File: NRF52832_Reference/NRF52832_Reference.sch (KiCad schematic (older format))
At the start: 49 parts

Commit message: Added breakout pins for SWDIO and SWDCLK for test purposes.
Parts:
- added J?: Conn_01x02_Male, symbol Connector:Conn_01x02_Male
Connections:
- net Sheet5BF15571/SWDCLK renamed SWDCLK
- net SWDCLK: now also J?.2 (Pin_2)
- net Sheet5BF15571/SWDIO renamed SWDIO
- net SWDIO: now also J?.1 (Pin_1)
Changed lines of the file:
@@
 NoConn ~ 7875 3800
 Wire Wire Line
-	9625 4300 9625 3600
+	9625 4300 9625 3675
 Wire Wire Line
 	9325 4300 9175 4300
@@
 Connection ~ 9625 4300
 Wire Wire Line
-	9750 5100 9750 3500
+	9750 5100 9750 3775
 Wire Notes Line
 	475  2575 11225 2575
@@
 Text Notes 3900 650  0    50   ~ 0
 GPIO and Button/LEDs
+$Comp
+L Connector:Conn_01x02_Male J?
+U 1 1 5C377AB0
+P 10475 3775
+F 0 "J?" H 10447 3701 50  0000 R CNN
+F 1 "Conn_01x02_Male" H 10448 3746 50  0001 R CNN
+F 2 "" H 10475 3775 50  0001 C CNN
+F 3 "~" H 10475 3775 50  0001 C CNN
+	1    10475 3775
+	-1   0    0    1
+$EndComp
+Wire Wire Line
+	10275 3675 9625 3675
+Connection ~ 9625 3675
+Wire Wire Line
+	9625 3675 9625 3600
+Wire Wire Line
+	10275 3775 9750 3775
+Connection ~ 9750 3775
+Wire Wire Line
+	9750 3775 9750 3500
+Text Label 9850 3675 0    50   ~ 0
+SWDCLK
+Text Label 9850 3775 0    50   ~ 0
+SWDIO
 $EndSCHEMATC

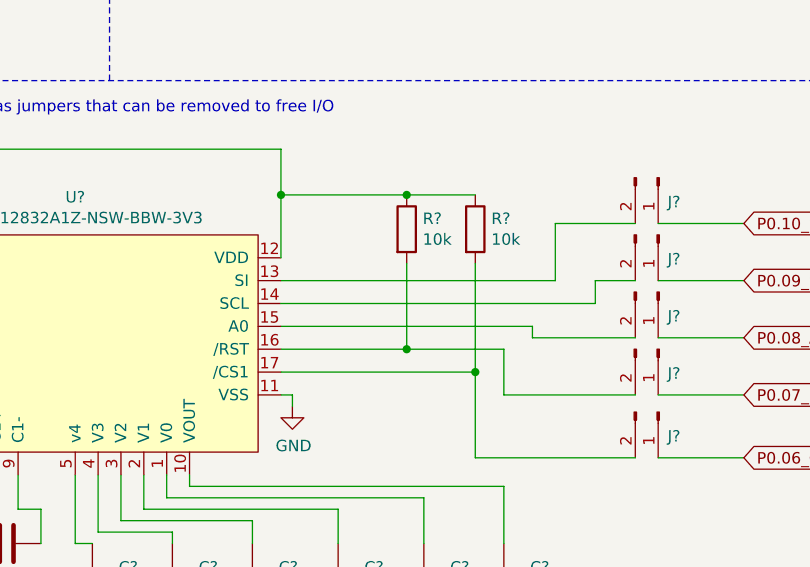
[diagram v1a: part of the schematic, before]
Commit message: Finished boost converter and regulators footprint assignments.
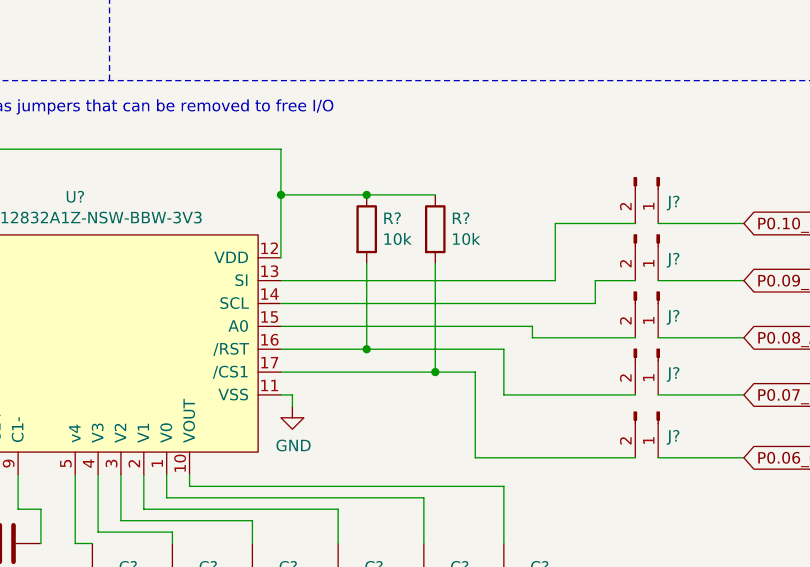
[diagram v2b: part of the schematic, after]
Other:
- moved on the sheet: R?
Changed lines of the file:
@@
 L Device:R R?
 U 1 1 5C0CAB0C
-P 4175 3225
-F 0 "R?" H 4245 3271 50  0000 L CNN
-F 1 "10k" H 4245 3180 50  0000 L CNN
-F 2 "" V 4105 3225 50  0001 C CNN
-F 3 "~" H 4175 3225 50  0001 C CNN
-	1    4175 3225
+P 4000 3225
+F 0 "R?" H 4070 3271 50  0000 L CNN
+F 1 "10k" H 4070 3180 50  0000 L CNN
+F 2 "" V 3930 3225 50  0001 C CNN
+F 3 "~" H 4000 3225 50  0001 C CNN
+	1    4000 3225
 	1    0    0    -1
 $EndComp
@@
 L Device:R R?
 U 1 1 5C0CAB88
-P 4475 3225
-F 0 "R?" H 4545 3271 50  0000 L CNN
-F 1 "10k" H 4545 3180 50  0000 L CNN
-F 2 "" V 4405 3225 50  0001 C CNN
-F 3 "~" H 4475 3225 50  0001 C CNN
-	1    4475 3225
-	1    0    0    -1
-$EndComp
-Wire Wire Line
-	3625 3850 4475 3850
-Wire Wire Line
-	3625 3750 4175 3750
+P 4300 3225
+F 0 "R?" H 4370 3271 50  0000 L CNN
+F 1 "10k" H 4370 3180 50  0000 L CNN
+F 2 "" V 4230 3225 50  0001 C CNN
+F 3 "~" H 4300 3225 50  0001 C CNN
+	1    4300 3225
+	1    0    0    -1
+$EndComp
+Wire Wire Line
+	3625 3850 4300 3850
+Wire Wire Line
+	3625 3750 4000 3750
 Text GLabel 5650 4225 2    50   Input ~ 0
 P0.06_CS1
@@
 P0.10_SI
 Wire Wire Line
-	4175 3750 4175 3375
+	4000 3750 4000 3375
 Wire Wire Line
 	3625 3350 3625 3075
 Wire Wire Line
-	3625 3075 4175 3075
-Connection ~ 4175 3075
-Wire Wire Line
-	4175 3075 4475 3075
+	3625 3075 4000 3075
 Wire Wire Line
 	8375 3900 8500 3900
@@
 	1100 2875 1100 2925
 Wire Wire Line
-	4475 3375 4475 3850
+	4300 3375 4300 3850
 $Comp
 L Connector:Conn_01x02_Male J?
@@
 Wire Wire Line
 	4475 4225 5175 4225
-Connection ~ 4475 3850
-Wire Wire Line
-	4175 3750 4600 3750
 Wire Wire Line
 	4600 3750 4600 3950
 Wire Wire Line
 	4600 3950 5175 3950
-Connection ~ 4175 3750
 Wire Wire Line
 	3625 3650 4725 3650
@@
 Text Label 9850 3775 0    50   ~ 0
 SWDIO
+Connection ~ 4000 3075
+Connection ~ 4000 3750
+Connection ~ 4300 3850
+Wire Wire Line
+	4300 3850 4475 3850
+Wire Wire Line
+	4000 3075 4300 3075
+Wire Wire Line
+	4000 3750 4600 3750
 $EndSCHEMATC

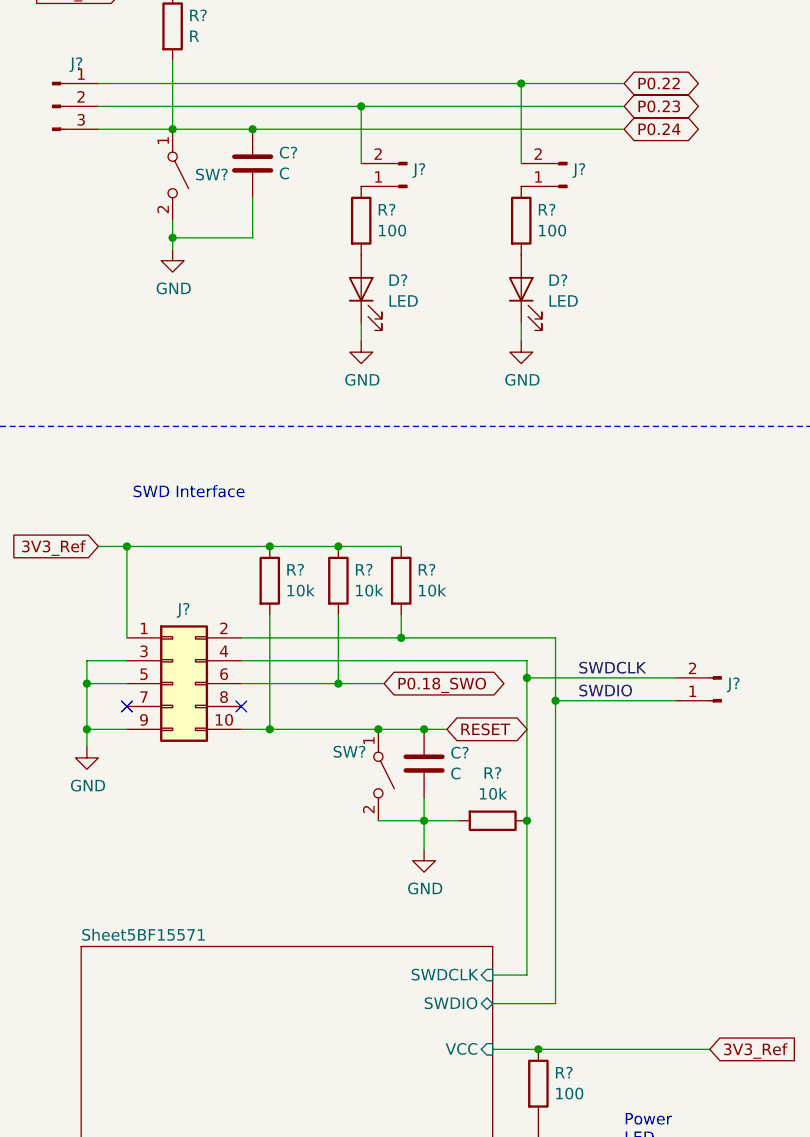
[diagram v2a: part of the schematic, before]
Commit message: Added footprint for LCD and finished footprint assignments for LCD components.
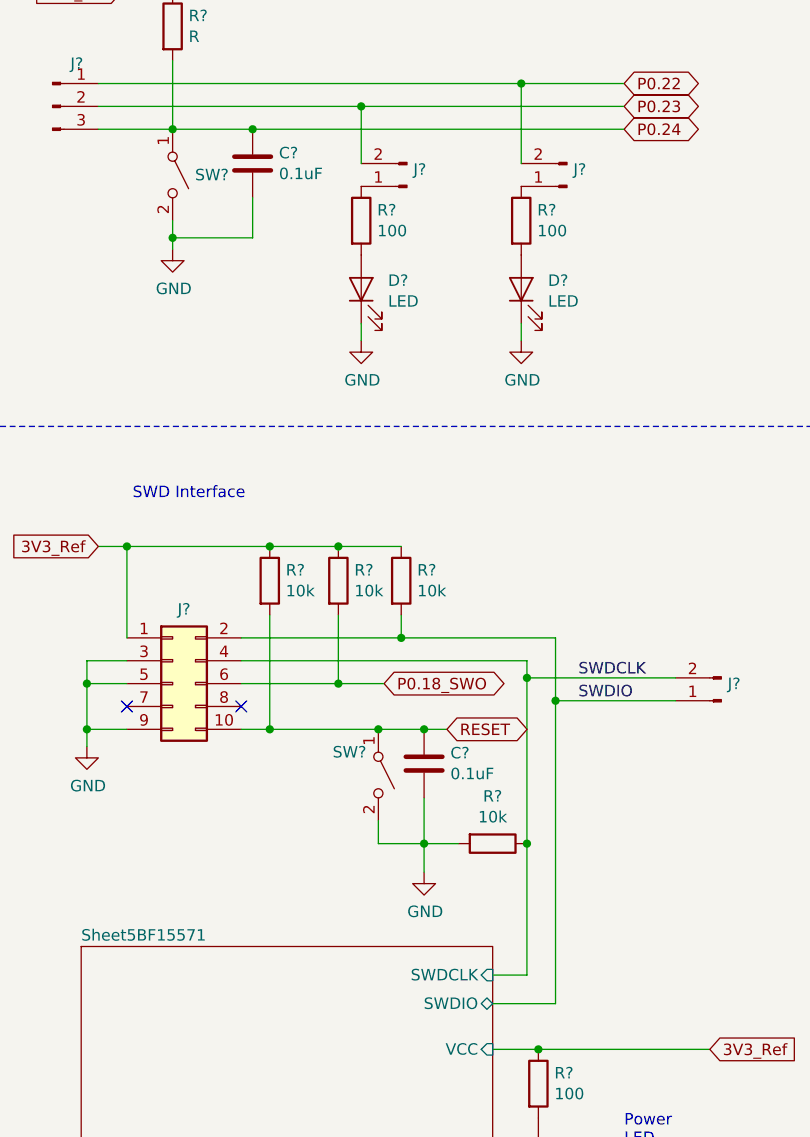
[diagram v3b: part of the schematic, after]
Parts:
- C? (x2): value C -> 0.1uF
- C? (x8): footprint (none) -> Capacitor_SMD:C_0603_1608Metric_Pad1.05x0.95mm_HandSolder
- J? (x5): footprint (none) -> Connector_PinHeader_2.54mm:PinHeader_1x02_P2.54mm_Vertical
- R? (x2): footprint (none) -> Resistor_SMD:R_0603_1608Metric_Pad1.05x0.95mm_HandSolder
- U?: footprint (none) -> Custom_Footprints:LCD_NHD-C12832A1Z-NSW-BBW-3V3
- U?: footprint (none) -> Custom_Footprints:SW_DPDT_Slide_JS202011CQN
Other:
- moved on the sheet: R?
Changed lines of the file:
@@
 P 9175 4050
 F 0 "C?" H 9290 4096 50  0000 L CNN
-F 1 "C" H 9290 4005 50  0000 L CNN
+F 1 "0.1uF" H 9290 4005 50  0000 L CNN
 F 2 "" H 9213 3900 50  0001 C CNN
 F 3 "~" H 9175 4050 50  0001 C CNN
@@
 L power:GND #PWR?
 U 1 1 5C0A6FF1
-P 9175 4425
-F 0 "#PWR?" H 9175 4175 50  0001 C CNN
-F 1 "GND" H 9180 4252 50  0000 C CNN
-F 2 "" H 9175 4425 50  0001 C CNN
-F 3 "" H 9175 4425 50  0001 C CNN
-	1    9175 4425
+P 9175 4525
+F 0 "#PWR?" H 9175 4275 50  0001 C CNN
+F 1 "GND" H 9180 4352 50  0000 C CNN
+F 2 "" H 9175 4525 50  0001 C CNN
+F 3 "" H 9175 4525 50  0001 C CNN
+	1    9175 4525
 	1    0    0    -1
 $EndComp
@@
 	9175 3900 9275 3900
 Wire Wire Line
-	8975 4300 9175 4300
-Wire Wire Line
-	9175 4300 9175 4425
-Wire Wire Line
-	9175 4200 9175 4300
-Connection ~ 9175 4300
+	8975 4400 9175 4400
+Wire Wire Line
+	9175 4400 9175 4525
+Connection ~ 9175 4400
 $Comp
 L Connector_Generic:Conn_02x05_Odd_Even J?
@@
 L Device:R R?
 U 1 1 5C0BEEFE
-P 9475 4300
-F 0 "R?" V 9268 4300 50  0000 C CNN
-F 1 "10k" V 9359 4300 50  0000 C CNN
-F 2 "" V 9405 4300 50  0001 C CNN
-F 3 "~" H 9475 4300 50  0001 C CNN
-	1    9475 4300
+P 9475 4400
+F 0 "R?" V 9268 4400 50  0000 C CNN
+F 1 "10k" V 9359 4400 50  0000 C CNN
+F 2 "" V 9405 4400 50  0001 C CNN
+F 3 "~" H 9475 4400 50  0001 C CNN
+	1    9475 4400
 	0    1    1    0
 $EndComp
 NoConn ~ 7875 3800
 Wire Wire Line
-	9625 4300 9625 3675
-Wire Wire Line
-	9325 4300 9175 4300
+	9325 4400 9175 4400
 Wire Wire Line
 	8800 3700 8800 3400
@@
 F 0 "U?" H 2725 4015 50  0000 C CNN
 F 1 "NHD-C12832A1Z-NSW-BBW-3V3" H 2725 3924 50  0000 C CNN
-F 2 "" H 2725 4300 50  0001 C CNN
+F 2 "Custom_Footprints:LCD_NHD-C12832A1Z-NSW-BBW-3V3" H 2725 4300 50  0001 C CNN
 F 3 "" H 2725 4300 50  0001 C CNN
 	1    2725 3550
@@
 F 0 "C?" V 2100 4500 50  0000 C CNN
 F 1 "1uF" V 2100 4650 50  0000 C CNN
-F 2 "" H 1938 4450 50  0001 C CNN
+F 2 "Capacitor_SMD:C_0603_1608Metric_Pad1.05x0.95mm_HandSolder" H 1938 4450 50  0001 C CNN
 F 3 "~" H 1900 4600 50  0001 C CNN
 	1    1900 4600
@@
 F 0 "C?" V 2625 4500 50  0000 C CNN
 F 1 "1uF" V 2625 4650 50  0000 C CNN
-F 2 "" H 2463 4450 50  0001 C CNN
+F 2 "Capacitor_SMD:C_0603_1608Metric_Pad1.05x0.95mm_HandSolder" H 2463 4450 50  0001 C CNN
 F 3 "~" H 2425 4600 50  0001 C CNN
 	1    2425 4600
@@
 F 0 "C?" H 2915 4796 50  0000 L CNN
 F 1 "1uF" H 2915 4705 50  0000 L CNN
-F 2 "" H 2838 4600 50  0001 C CNN
+F 2 "Capacitor_SMD:C_0603_1608Metric_Pad1.05x0.95mm_HandSolder" H 2838 4600 50  0001 C CNN
 F 3 "~" H 2800 4750 50  0001 C CNN
 	1    2800 4750
@@
 F 0 "C?" H 3265 4796 50  0000 L CNN
 F 1 "1uF" H 3265 4705 50  0000 L CNN
-F 2 "" H 3188 4600 50  0001 C CNN
+F 2 "Capacitor_SMD:C_0603_1608Metric_Pad1.05x0.95mm_HandSolder" H 3188 4600 50  0001 C CNN
 F 3 "~" H 3150 4750 50  0001 C CNN
 	1    3150 4750
@@
 F 0 "C?" H 3615 4796 50  0000 L CNN
 F 1 "1uF" H 3615 4705 50  0000 L CNN
-F 2 "" H 3538 4600 50  0001 C CNN
+F 2 "Capacitor_SMD:C_0603_1608Metric_Pad1.05x0.95mm_HandSolder" H 3538 4600 50  0001 C CNN
 F 3 "~" H 3500 4750 50  0001 C CNN
 	1    3500 4750
@@
 F 0 "C?" H 3990 4796 50  0000 L CNN
 F 1 "1uF" H 3990 4705 50  0000 L CNN
-F 2 "" H 3913 4600 50  0001 C CNN
+F 2 "Capacitor_SMD:C_0603_1608Metric_Pad1.05x0.95mm_HandSolder" H 3913 4600 50  0001 C CNN
 F 3 "~" H 3875 4750 50  0001 C CNN
 	1    3875 4750
@@
 F 0 "C?" H 4365 4796 50  0000 L CNN
 F 1 "1uF" H 4365 4705 50  0000 L CNN
-F 2 "" H 4288 4600 50  0001 C CNN
+F 2 "Capacitor_SMD:C_0603_1608Metric_Pad1.05x0.95mm_HandSolder" H 4288 4600 50  0001 C CNN
 F 3 "~" H 4250 4750 50  0001 C CNN
 	1    4250 4750
@@
 F 0 "C?" H 4715 4796 50  0000 L CNN
 F 1 "1uF" H 4715 4705 50  0000 L CNN
-F 2 "" H 4638 4600 50  0001 C CNN
+F 2 "Capacitor_SMD:C_0603_1608Metric_Pad1.05x0.95mm_HandSolder" H 4638 4600 50  0001 C CNN
 F 3 "~" H 4600 4750 50  0001 C CNN
 	1    4600 4750
@@
 F 0 "R?" H 4070 3271 50  0000 L CNN
 F 1 "10k" H 4070 3180 50  0000 L CNN
-F 2 "" V 3930 3225 50  0001 C CNN
+F 2 "Resistor_SMD:R_0603_1608Metric_Pad1.05x0.95mm_HandSolder" V 3930 3225 50  0001 C CNN
 F 3 "~" H 4000 3225 50  0001 C CNN
 	1    4000 3225
@@
 F 0 "R?" H 4370 3271 50  0000 L CNN
 F 1 "10k" H 4370 3180 50  0000 L CNN
-F 2 "" V 4230 3225 50  0001 C CNN
+F 2 "Resistor_SMD:R_0603_1608Metric_Pad1.05x0.95mm_HandSolder" V 4230 3225 50  0001 C CNN
 F 3 "~" H 4300 3225 50  0001 C CNN
 	1    4300 3225
@@
 F 0 "U?" H 1352 3146 50  0000 L CNN
 F 1 "SLIDE_SW_DPDT" H 1352 3055 50  0000 L CNN
-F 2 "" H 1200 3350 50  0001 C CNN
+F 2 "Custom_Footprints:SW_DPDT_Slide_JS202011CQN" H 1200 3350 50  0001 C CNN
 F 3 "" H 1200 3350 50  0001 C CNN
 	1    1200 3100
@@
 F 0 "J?" V 5381 3041 50  0000 L CNN
 F 1 "Conn_01x02_Male" V 5426 3040 50  0001 L CNN
-F 2 "" H 5275 3000 50  0001 C CNN
+F 2 "Connector_PinHeader_2.54mm:PinHeader_1x02_P2.54mm_Vertical" H 5275 3000 50  0001 C CNN
 F 3 "~" H 5275 3000 50  0001 C CNN
 	1    5275 3000
@@
 F 0 "J?" V 5381 3291 50  0000 L CNN
 F 1 "Conn_01x02_Male" V 5426 3290 50  0001 L CNN
-F 2 "" H 5275 3250 50  0001 C CNN
+F 2 "Connector_PinHeader_2.54mm:PinHeader_1x02_P2.54mm_Vertical" H 5275 3250 50  0001 C CNN
 F 3 "~" H 5275 3250 50  0001 C CNN
 	1    5275 3250
@@
 F 0 "J?" V 5381 3541 50  0000 L CNN
 F 1 "Conn_01x02_Male" V 5426 3540 50  0001 L CNN
-F 2 "" H 5275 3500 50  0001 C CNN
+F 2 "Connector_PinHeader_2.54mm:PinHeader_1x02_P2.54mm_Vertical" H 5275 3500 50  0001 C CNN
 F 3 "~" H 5275 3500 50  0001 C CNN
 	1    5275 3500
@@
 F 0 "J?" V 5381 3791 50  0000 L CNN
 F 1 "Conn_01x02_Male" V 5426 3790 50  0001 L CNN
-F 2 "" H 5275 3750 50  0001 C CNN
+F 2 "Connector_PinHeader_2.54mm:PinHeader_1x02_P2.54mm_Vertical" H 5275 3750 50  0001 C CNN
 F 3 "~" H 5275 3750 50  0001 C CNN
 	1    5275 3750
@@
 F 0 "J?" V 5381 4066 50  0000 L CNN
 F 1 "Conn_01x02_Male" V 5426 4065 50  0001 L CNN
-F 2 "" H 5275 4025 50  0001 C CNN
+F 2 "Connector_PinHeader_2.54mm:PinHeader_1x02_P2.54mm_Vertical" H 5275 4025 50  0001 C CNN
 F 3 "~" H 5275 4025 50  0001 C CNN
 	1    5275 4025
@@
 P 8425 1425
 F 0 "C?" H 8540 1471 50  0000 L CNN
-F 1 "C" H 8540 1380 50  0000 L CNN
+F 1 "0.1uF" H 8540 1380 50  0000 L CNN
 F 2 "" H 8463 1275 50  0001 C CNN
 F 3 "~" H 8425 1425 50  0001 C CNN
@@
 	9600 2125 9600 2200
 Wire Wire Line
-	9625 4975 9625 4300
-Connection ~ 9625 4300
+	9625 4975 9625 4400
 Wire Wire Line
 	9750 5100 9750 3775
@@
 Wire Wire Line
 	4000 3750 4600 3750
+Connection ~ 9625 4400
+Wire Wire Line
+	9625 3675 9625 4400
+Wire Wire Line
+	8975 4400 8975 4300
+Wire Wire Line
+	9175 4200 9175 4400
 $EndSCHEMATC

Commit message: Finished footprint assignments for I2C components
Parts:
- C? (x3): footprint (none) -> Capacitor_SMD:C_0603_1608Metric_Pad1.05x0.95mm_HandSolder
- J? (x2): footprint (none) -> Connector_PinHeader_2.54mm:PinHeader_1x02_P2.54mm_Vertical
- R? (x2): footprint (none) -> Resistor_SMD:R_0603_1608Metric_Pad1.05x0.95mm_HandSolder
- U?: footprint (none) -> Package_SO:TSSOP-8_4.4x3mm_P0.65mm
- U?: footprint (none) -> Custom_Footprints:Sensor_Photo_LTR-329ALS-01
- U?: footprint (none) -> Package_SO:MSOP-8_3x3mm_P0.65mm
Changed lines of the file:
@@
 F 0 "U?" H 1675 6665 50  0000 C CNN
 F 1 "AT34C04-X5M-T" H 1675 6574 50  0000 C CNN
-F 2 "" H 1625 6850 50  0001 C CNN
+F 2 "Package_SO:TSSOP-8_4.4x3mm_P0.65mm" H 1625 6850 50  0001 C CNN
 F 3 "" H 1625 6850 50  0001 C CNN
 	1    1675 6350
@@
 F 0 "U?" H 3000 6915 50  0000 C CNN
 F 1 "LTR-329ALS-01" H 3000 6824 50  0000 C CNN
-F 2 "" H 3000 6650 50  0001 C CNN
+F 2 "Custom_Footprints:Sensor_Photo_LTR-329ALS-01" H 3000 6650 50  0001 C CNN
 F 3 "" H 3000 6650 50  0001 C CNN
 	1    3000 6550
@@
 F 0 "U?" H 4425 6965 50  0000 C CNN
 F 1 "TCN75AVUA713" H 4425 6874 50  0000 C CNN
-F 2 "" H 4475 6950 50  0001 C CNN
+F 2 "Package_SO:MSOP-8_3x3mm_P0.65mm" H 4475 6950 50  0001 C CNN
 F 3 "" H 4475 6950 50  0001 C CNN
 	1    4425 6500
@@
 F 0 "C?" H 2350 6700 50  0000 L CNN
 F 1 "0.1uF" H 2275 6600 50  0000 L CNN
-F 2 "" H 2613 6500 50  0001 C CNN
+F 2 "Capacitor_SMD:C_0603_1608Metric_Pad1.05x0.95mm_HandSolder" H 2613 6500 50  0001 C CNN
 F 3 "~" H 2575 6650 50  0001 C CNN
 	1    2575 6650
@@
 F 0 "C?" H 3550 6450 50  0000 L CNN
 F 1 "0.1uF" H 3525 6350 50  0000 L CNN
-F 2 "" H 3813 6300 50  0001 C CNN
+F 2 "Capacitor_SMD:C_0603_1608Metric_Pad1.05x0.95mm_HandSolder" H 3813 6300 50  0001 C CNN
 F 3 "~" H 3775 6450 50  0001 C CNN
 	1    3775 6450
@@
 F 0 "R?" H 5345 7046 50  0000 L CNN
 F 1 "10k" H 5345 6955 50  0000 L CNN
-F 2 "" V 5205 7000 50  0001 C CNN
+F 2 "Resistor_SMD:R_0603_1608Metric_Pad1.05x0.95mm_HandSolder" V 5205 7000 50  0001 C CNN
 F 3 "~" H 5275 7000 50  0001 C CNN
 	1    5275 7000
@@
 F 0 "R?" H 5645 7046 50  0000 L CNN
 F 1 "10k" H 5645 6955 50  0000 L CNN
-F 2 "" V 5505 7000 50  0001 C CNN
+F 2 "Resistor_SMD:R_0603_1608Metric_Pad1.05x0.95mm_HandSolder" V 5505 7000 50  0001 C CNN
 F 3 "~" H 5575 7000 50  0001 C CNN
 	1    5575 7000
@@
 F 0 "J?" V 6056 7091 50  0000 L CNN
 F 1 "Conn_01x02_Male" V 6101 7090 50  0001 L CNN
-F 2 "" H 5950 7050 50  0001 C CNN
+F 2 "Connector_PinHeader_2.54mm:PinHeader_1x02_P2.54mm_Vertical" H 5950 7050 50  0001 C CNN
 F 3 "~" H 5950 7050 50  0001 C CNN
 	1    5950 7050
@@
 F 0 "J?" V 6025 7525 50  0000 R CNN
 F 1 "Conn_01x02_Male" V 6012 7513 50  0001 R CNN
-F 2 "" H 5950 7700 50  0001 C CNN
+F 2 "Connector_PinHeader_2.54mm:PinHeader_1x02_P2.54mm_Vertical" H 5950 7700 50  0001 C CNN
 F 3 "~" H 5950 7700 50  0001 C CNN
 	1    5950 7700
@@
 F 0 "C?" H 875 6500 50  0000 L CNN
 F 1 "0.1uF" H 775 6400 50  0000 L CNN
-F 2 "" H 1138 6300 50  0001 C CNN
+F 2 "Capacitor_SMD:C_0603_1608Metric_Pad1.05x0.95mm_HandSolder" H 1138 6300 50  0001 C CNN
 F 3 "~" H 1100 6450 50  0001 C CNN
 	1    1100 6450
